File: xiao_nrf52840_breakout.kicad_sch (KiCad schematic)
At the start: 12 parts, among them J1 53261-0271, J10 Conn_01x01, J2 Conn_01x07, J3 Conn_01x07, J4 Conn_01x01, J5 Conn_01x03, J6 Conn_02x02_Odd_Even, J7 Conn_01x03, J8 Conn_01x01, J9 Conn_01x01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

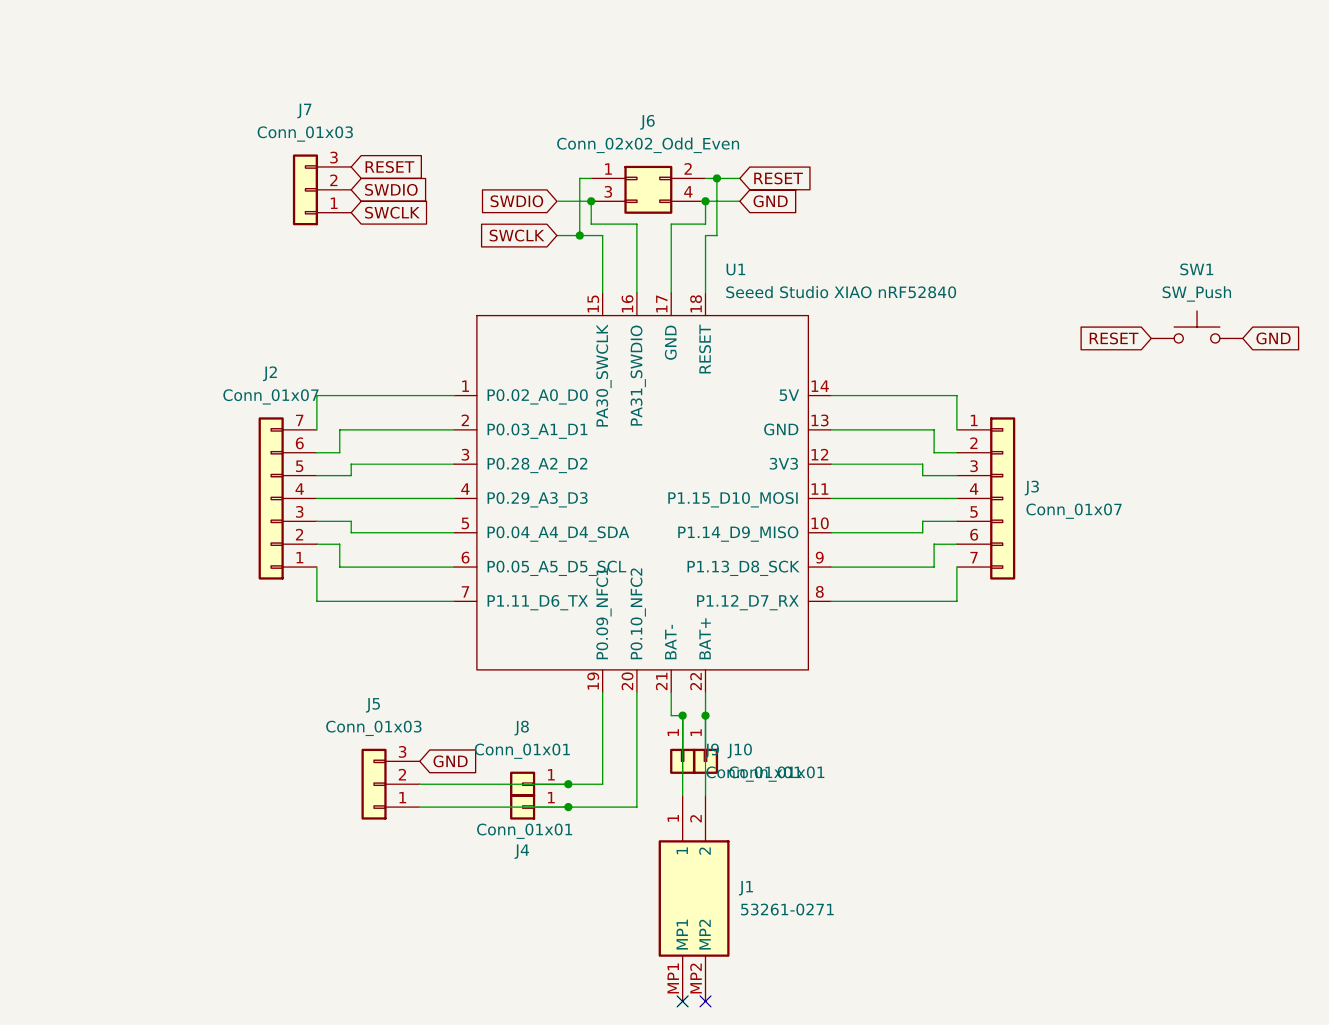
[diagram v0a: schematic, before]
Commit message: add extra bat+ and bat- pins
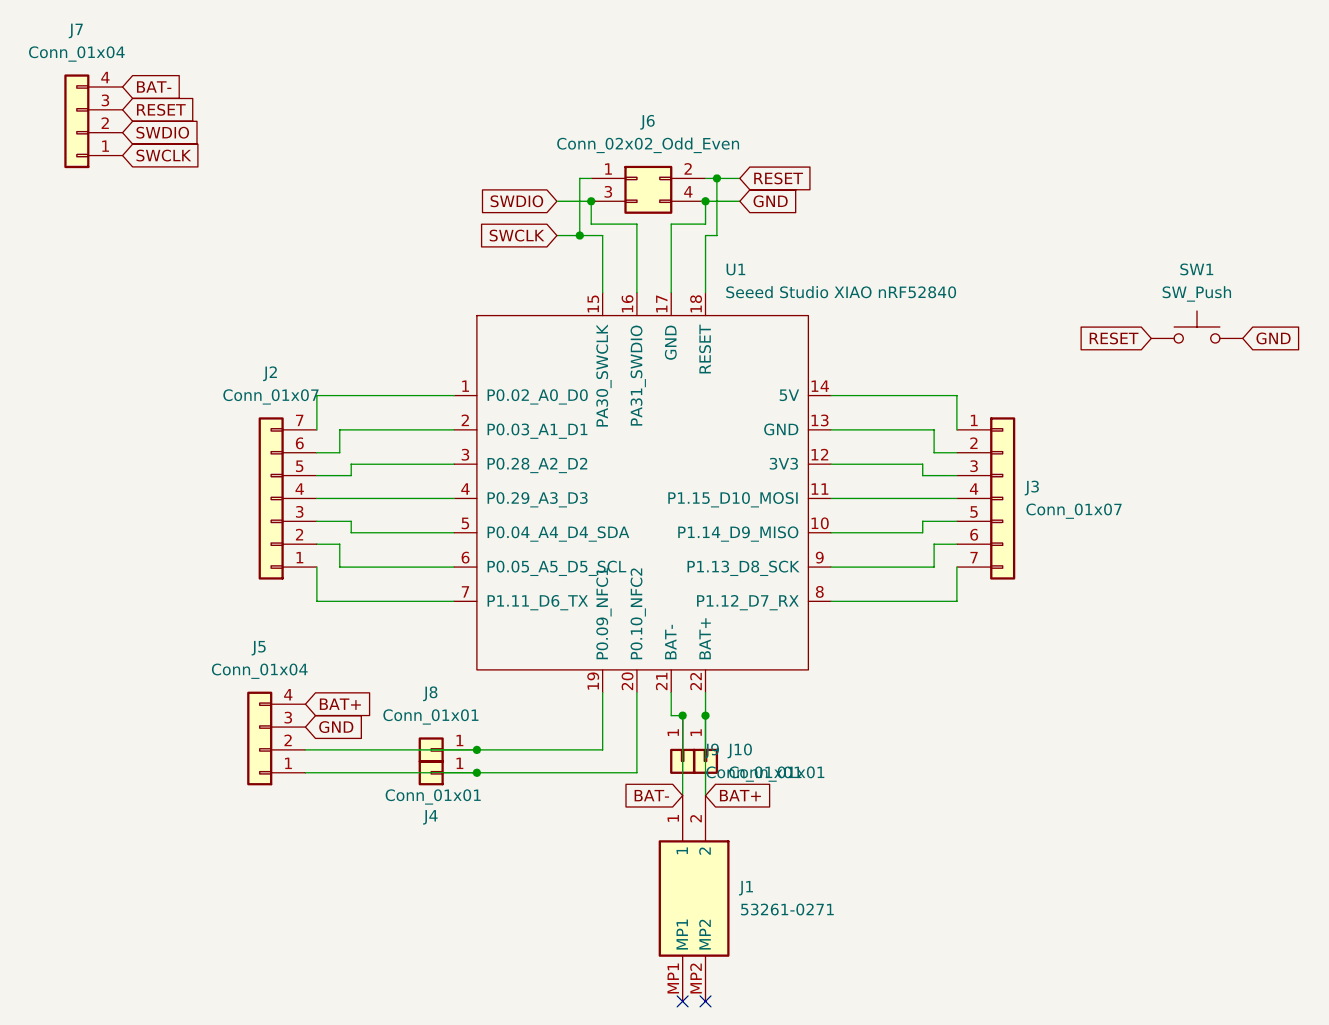
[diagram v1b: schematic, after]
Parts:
- removed J5, J7: Conn_01x03, Connector_PinSocket_2.54mm:PinSocket_1x03_P2.54mm_Vertical, symbol Connector_Generic:Conn_01x03
- added J5, J7: Conn_01x04, Connector_PinSocket_2.54mm:PinSocket_1x04_P2.54mm_Vertical, symbol Connector_Generic:Conn_01x04
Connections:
- net GND: now also J5.3 (Pin_3)
- net RESET: now also J7.3 (Pin_3)
- net SWCLK: now also J7.1 (Pin_1)
- net SWDIO: now also J7.2 (Pin_2)
- net at J8.1 (Pin_1), U1.19 (P0.09_NFC1): now also J5.2 (Pin_2)
- net at J4.1 (Pin_1), U1.20 (P0.10_NFC2): now also J5.1 (Pin_1)
- net BAT+: now reaches J1.2, J10.1 (Pin_1), U1.22 (BAT+)
- net BAT+: now also J5.4 (Pin_4)
- net BAT-: now reaches J1.1, J9.1 (Pin_1), U1.21 (BAT-)
- net BAT-: now also J7.4 (Pin_4)
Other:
- moved on the sheet: J4, J8
